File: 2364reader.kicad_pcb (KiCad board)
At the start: 2 copper layers, 20.2 x 36.4 mm, 2 parts, among them U1 2364, U2 27C64

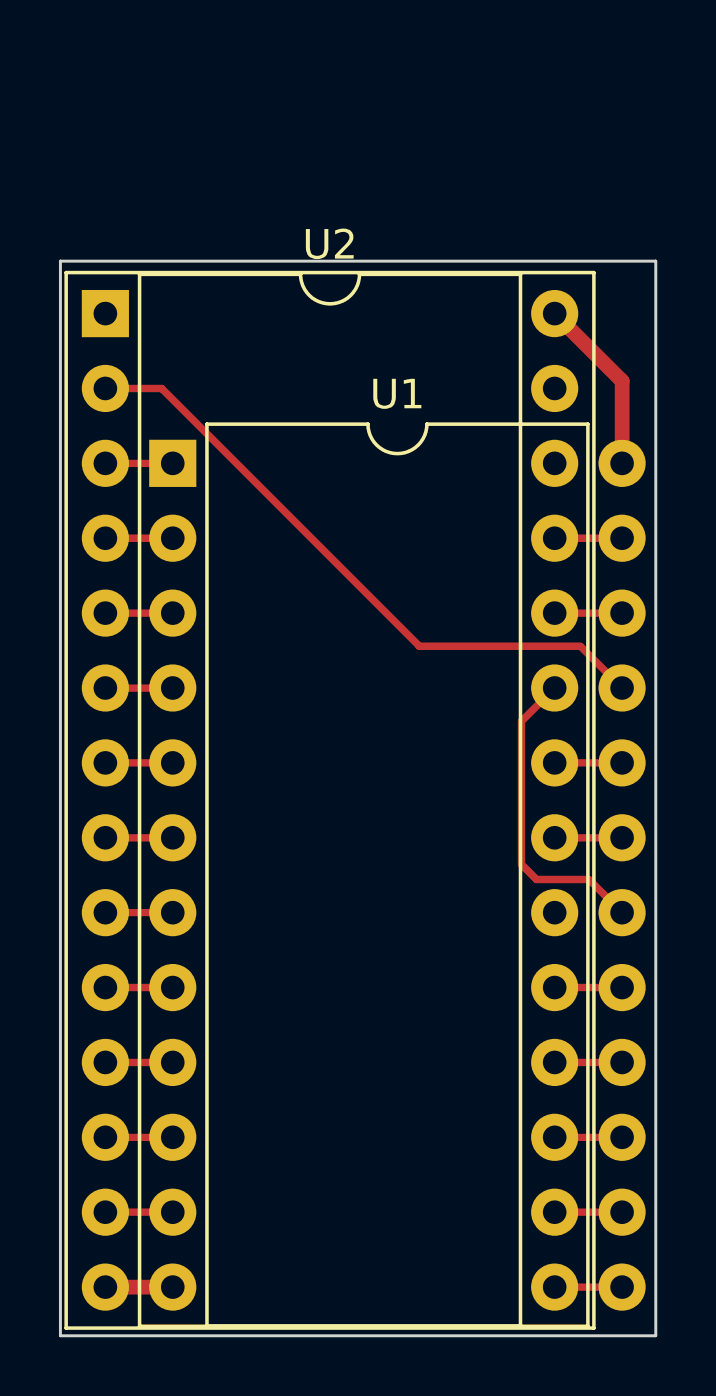
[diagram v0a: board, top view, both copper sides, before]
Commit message: adapt to accept 2332
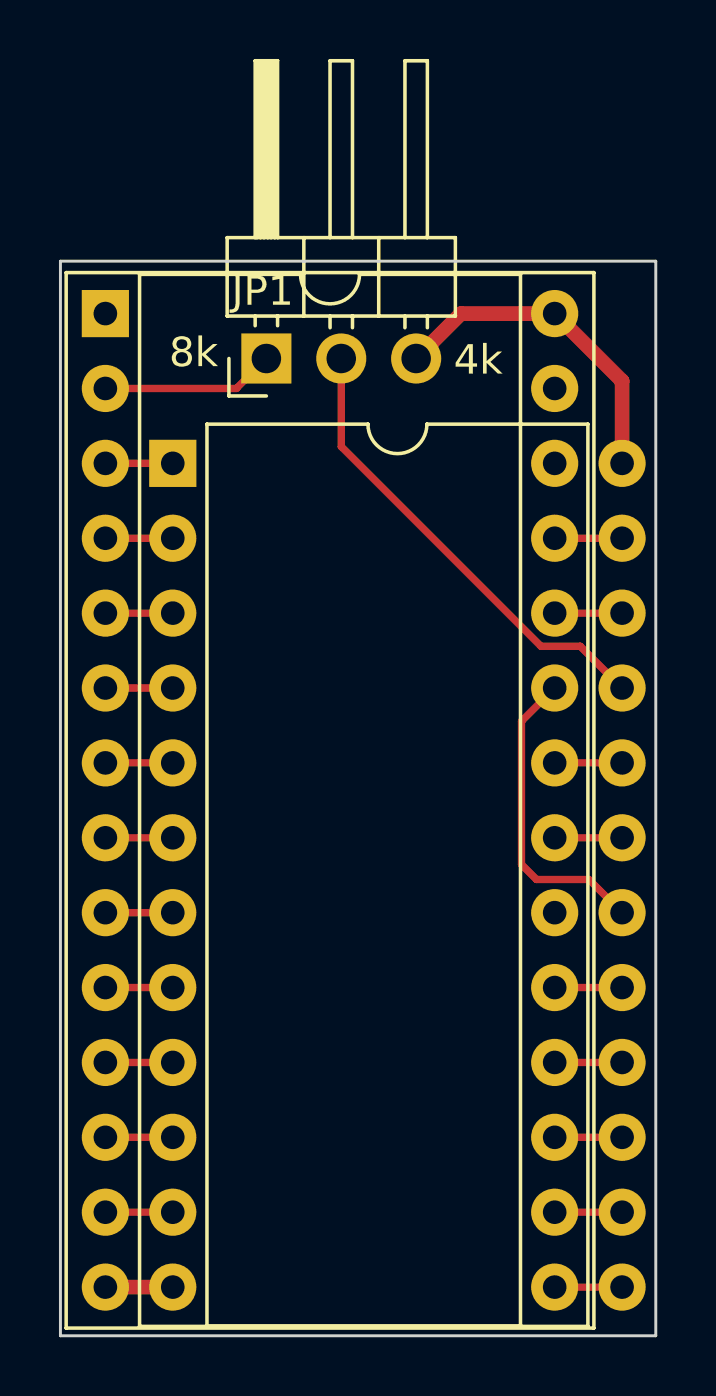
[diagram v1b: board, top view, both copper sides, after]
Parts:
- added JP1: 2364/2332, Connector_PinHeader_2.54mm:PinHeader_1x03_P2.54mm_Horizontal, F.Cu at (119.4, 59.6)
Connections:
- U1 pad 21: A12 -> RA12
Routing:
- net RA12: track 0.00 -> 15.9 mm
- net A12: track 21.7 -> 5.88 mm
- net +5V: track 6.03 -> 11.4 mm
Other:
- board text added: "4k"
- board text added: "8k"

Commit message: revise board to fix 2332 problem
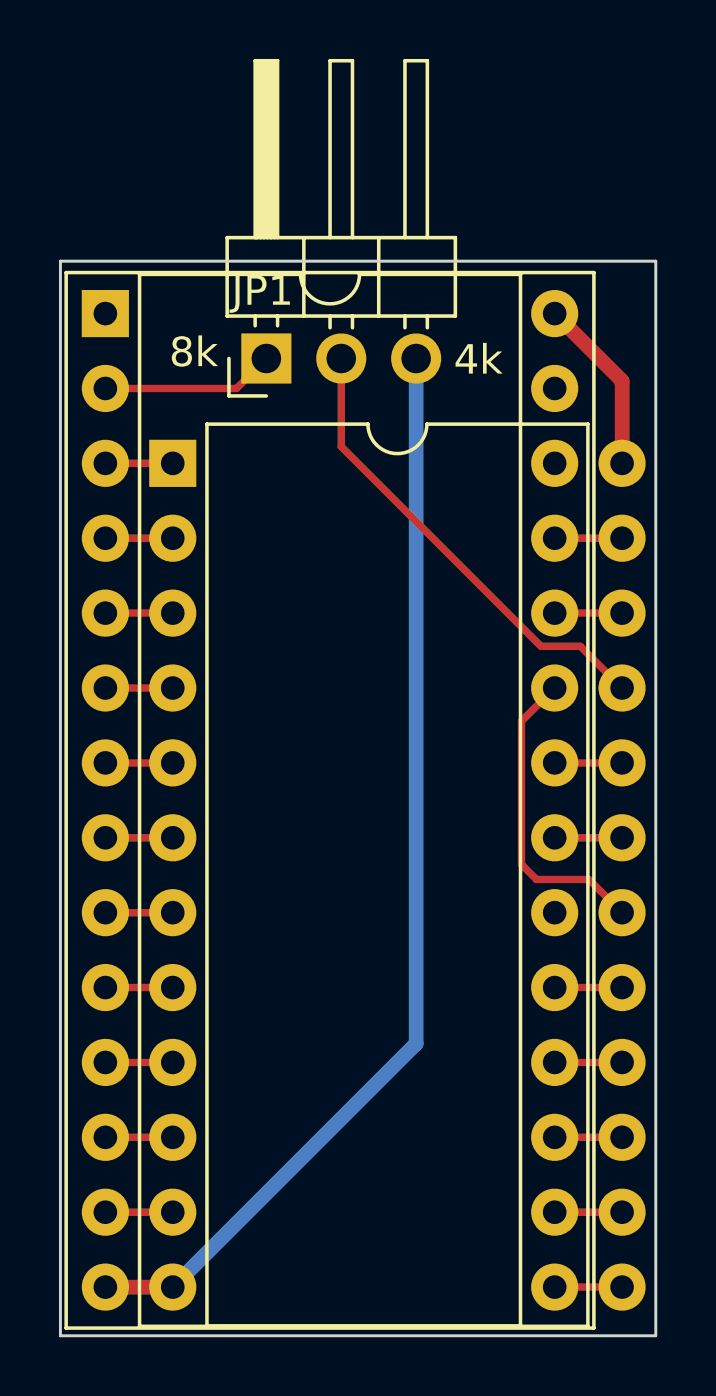
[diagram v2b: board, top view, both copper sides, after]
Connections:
- JP1 pad 3: +5V -> GND
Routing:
- net GND: track 2.29 -> 37.2 mm
- net +5V: track 11.4 -> 6.03 mm
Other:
- board text added: "2332/2364 masked rom adapter"
- board text added: "rev 2 by Julian Brown"
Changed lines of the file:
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@@
       (net 29 "RA12") (pinfunction "C") (pintype "passive"))
     (pad "3" thru_hole oval (at 0 5.08 90) (size 1.7 1.7) (drill 1) (layers "*.Cu" "*.Mask")
-      (net 24 "+5V") (pinfunction "B") (pintype "passive"))
+      (net 12 "GND") (pinfunction "B") (pintype "passive"))
     (model "${KICAD6_3DMODEL_DIR}/Connector_PinHeader_2.54mm.3dshapes/PinHeader_1x03_P2.54mm_Horizontal.wrl"
       (offset (xyz 0 0 0))
@@
   (gr_line (start 112.395 56.261) (end 132.588 56.261)
     (stroke (width 0.1) (type default)) (layer "Edge.Cuts"))
+  (gr_text "2332/2364 masked rom adapter" (at 119.4816 64.6684 90) (layer "B.SilkS")
+    (effects (font (size 1 1) (thickness 0.15)) (justify left bottom mirror))
+  )
+  (gr_text "rev 2 by Julian Brown" (at 121.2088 68.4276 90) (layer "B.SilkS")
+    (effects (font (size 1 1) (thickness 0.15)) (justify left bottom mirror))
+  )
   (gr_text "8k" (at 116.078 59.944) (layer "F.SilkS")
     (effects (font (size 1 1) (thickness 0.15)) (justify left bottom))
@@
   (segment (start 113.919 88.519) (end 116.205 88.519) (width 0.25) (layer "F.Cu") (net 11))
   (segment (start 113.919 91.059) (end 116.205 91.059) (width 0.5) (layer "F.Cu") (net 12))
+  (segment (start 116.205 91.059) (end 124.46 82.804) (width 0.5) (layer "B.Cu") (net 12))
+  (segment (start 124.46 82.804) (end 124.46 59.563) (width 0.5) (layer "B.Cu") (net 12))
   (segment (start 129.159 91.059) (end 131.445 91.059) (width 0.25) (layer "F.Cu") (net 13))
   (segment (start 131.445 88.519) (end 129.159 88.519) (width 0.25) (layer "F.Cu") (net 14))
@@
   (segment (start 129.159 68.199) (end 131.445 68.199) (width 0.25) (layer "F.Cu") (net 22))
   (segment (start 129.159 65.659) (end 131.445 65.659) (width 0.25) (layer "F.Cu") (net 23))
-  (segment (start 129.159 58.039) (end 125.984 58.039) (width 0.5) (layer "F.Cu") (net 24))
   (segment (start 129.159 58.039) (end 131.445 60.325) (width 0.5) (layer "F.Cu") (net 24))
-  (segment (start 125.984 58.039) (end 124.46 59.563) (width 0.5) (layer "F.Cu") (net 24))
   (segment (start 131.445 60.325) (end 131.445 63.119) (width 0.5) (layer "F.Cu") (net 24))
   (segment (start 128.693009 69.324) (end 121.92 62.550991) (width 0.25) (layer "F.Cu") (net 29))
